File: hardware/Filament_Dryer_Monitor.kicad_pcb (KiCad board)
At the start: 4 copper layers, 91 x 52 mm, 95 parts, among them J1 DC Connector, J2 USB_C_Receptacle_USB2.0_16P, J3 Sensor, J4 Display, J5 Heater Connector, J6 Fan Connector, J7 NTC Connector, Q1 DMP6180SK3-13, Q2 MMBT3904, Q3 MMBT3904, Q4 IRLR3636TRPBF, Q5 CJ2310, Q6 MMBT3904, U1 AP66200, U2 CP2102N-A02-GQFN28R, U3 USBLC6-2SC6, U4 ESP32-WROOM-32E-N4

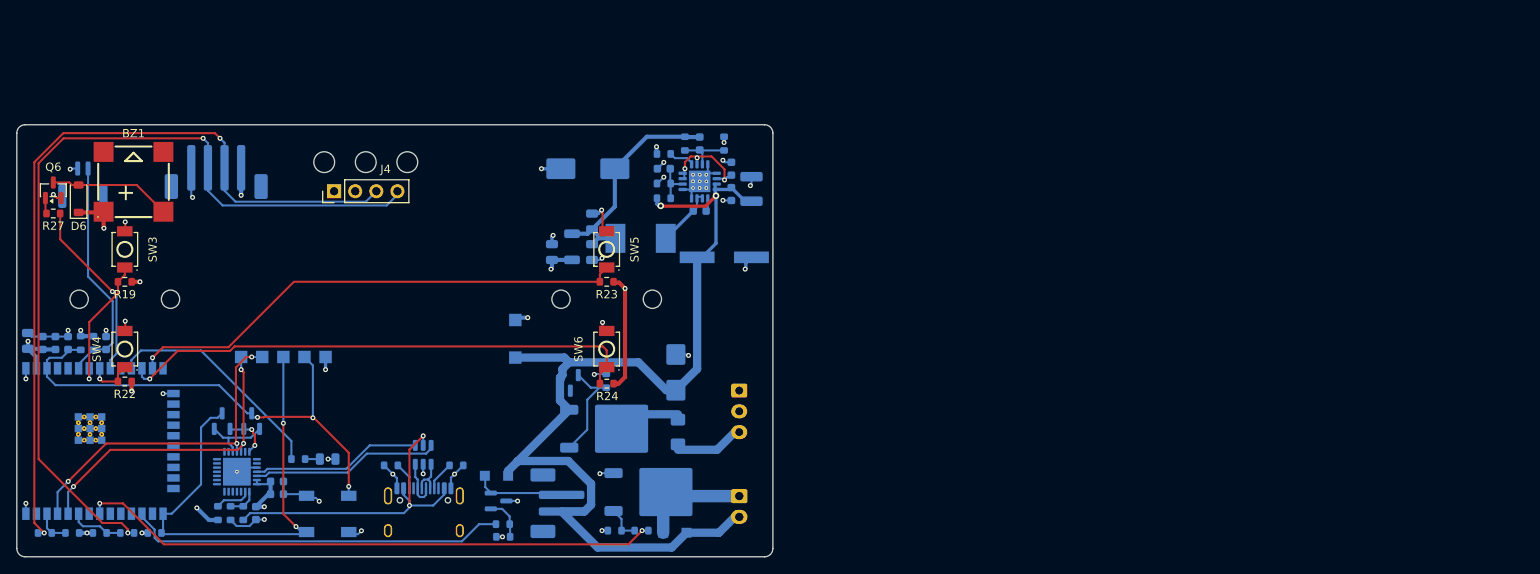
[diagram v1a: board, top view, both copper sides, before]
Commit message: Sync PCB with L7987L schematic
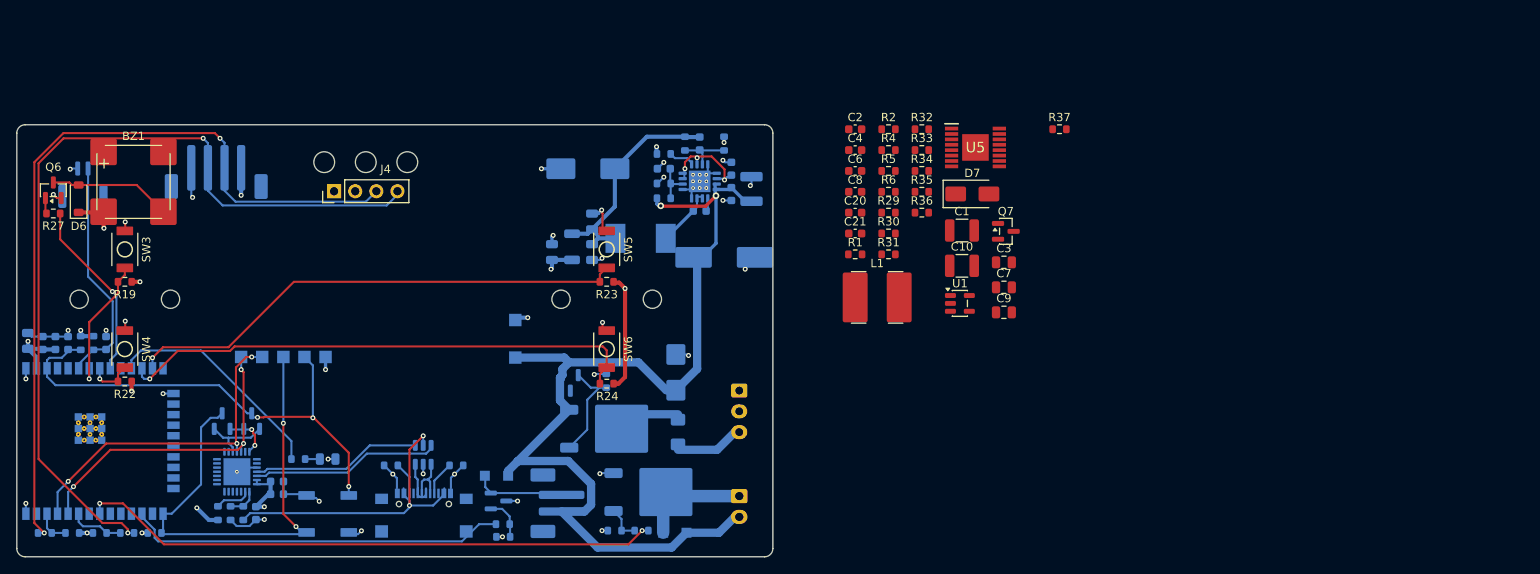
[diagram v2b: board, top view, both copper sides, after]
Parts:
- added C1: 10u, Capacitor_SMD:C_1210_3225Metric, F.Cu at (213.8, 92.7)
- added C10: 47u, Capacitor_SMD:C_1210_3225Metric, F.Cu at (213.8, 97.0)
- added C2: 100n, Capacitor_SMD:C_0603_1608Metric, F.Cu at (200.9, 80.5)
- added C20: 560p, Capacitor_SMD:C_0603_1608Metric, F.Cu at (200.9, 90.6)
- added C21: 1u, Capacitor_SMD:C_0603_1608Metric, F.Cu at (200.9, 93.1)
- added C3: 1u, Capacitor_SMD:C_0805_2012Metric, F.Cu at (218.8, 96.6)
- added C4: 33n, Capacitor_SMD:C_0603_1608Metric, F.Cu at (200.9, 83.0)
- added C6: 100n, Capacitor_SMD:C_0603_1608Metric, F.Cu at (200.9, 85.6)
- added C7: 330n, Capacitor_SMD:C_0805_2012Metric, F.Cu at (218.8, 99.6)
- added C8: 39p, Capacitor_SMD:C_0603_1608Metric, F.Cu at (200.9, 88.1)
- added C9: 18n, Capacitor_SMD:C_0805_2012Metric, F.Cu at (218.8, 102.6)
- added D7: STPS2L60A, Diode_SMD:D_SMA, F.Cu at (215.0, 88.3)
- added L1: 15u, FilamentDryer:L_Bourns_SRN6045, F.Cu at (203.6, 100.8)
- added Q7: MMBT3904, Package_TO_SOT_SMD:SOT-23, F.Cu at (219.0, 92.8)
- added R1: 270k, Resistor_SMD:R_0603_1608Metric, F.Cu at (200.9, 95.6)
- added R2: 22k, Resistor_SMD:R_0603_1608Metric, F.Cu at (204.9, 80.5)
- added R29: 47k5, Resistor_SMD:R_0603_1608Metric, F.Cu at (204.9, 90.6)
- added R30: 47k, Resistor_SMD:R_0603_1608Metric, F.Cu at (204.9, 93.1)
- added R31: 100k, Resistor_SMD:R_0603_1608Metric, F.Cu at (204.9, 95.6)
- added R32: 15k, Resistor_SMD:R_0603_1608Metric, F.Cu at (208.9, 80.5)
- added R33: 16k, Resistor_SMD:R_0603_1608Metric, F.Cu at (208.9, 83.0)
- added R34: 16k, Resistor_SMD:R_0603_1608Metric, F.Cu at (208.9, 85.6)
- added R35: 1k13, Resistor_SMD:R_0603_1608Metric, F.Cu at (208.9, 88.1)
- added R36: 49k9, Resistor_SMD:R_0603_1608Metric, F.Cu at (208.9, 90.6)
- added R37: 100k, Resistor_SMD:R_0603_1608Metric, F.Cu at (225.5, 80.5)
- added R4: 47k, Resistor_SMD:R_0603_1608Metric, F.Cu at (204.9, 83.0)
- added R5: 100k, Resistor_SMD:R_0603_1608Metric, F.Cu at (204.9, 85.6)
- added R6: 100k, Resistor_SMD:R_0603_1608Metric, F.Cu at (204.9, 88.1)
- added U1: TLV1701, Package_TO_SOT_SMD:SOT-23-5, F.Cu at (213.5, 101.5)
- added U5: L7987L, SamacSys_Parts:SOP65P640X120-17N, F.Cu at (215.4, 82.7)
- BZ1: value MLT-8530 -> LD-BZEL-T67-0808; footprint JLCPCB:BUZ-SMD_4P-L8.5-W8.5-P8.50-BR -> FilamentDryer:BUZ_Loudity_SMT67_8.5x8.5
- C5: footprint JLCPCB:CAP-SMD_BD8.0-L8.3-W8.3-FD -> FilamentDryer:CP_Panasonic_F_8x10.2
- D1: value BZX84C15 -> BZX84C15-7-F
- FB1: value HCB3216KF-601T30 -> BLM31KN601SH1L
- J2: footprint FilamentDryer:USB_C_Receptacle_HRO_TYPE-C-31-M-12 -> FilamentDryer:USB_C_GCT_USB4216-03-A
- Q1: value DMP6180SK3-13 -> NTD20P06LT4G
- Q5: value CJ2310 -> IRLML2060TRPBF
- SW1, SW2, SW3, SW4, SW5, SW6: footprint JLCPCB:SW-SMD_L3.9-W3.0-P4.45 -> FilamentDryer:SW_GCT_SWT0110
- U2: value CP2102N-A02-GQFN28R -> CP2102-GM; footprint FilamentDryer:CP2102N_GQFN28_5x5mm_P0.5mm_EP3.35x3.35mm -> FilamentDryer:CP2102_GM_QFN28_5x5_P0.5_EP3.25
- U3: value USBLC6-2SC6 -> AKS1201
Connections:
- D1 pad 1: 24V_PROT -> /Power/GATE_Q1
- D1 pad 2: /Power/GATE_Q1 -> unconnected-(D1-NC-Pad2)
- D1 pad 3: (no net) -> 24V_PROT
- Q5 pad 2: Net-(D5-A) -> GND
- Q5 pad 3: GND -> Net-(D5-A)
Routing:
- net Net-(D5-A): track 11.0 -> 12.3 mm, vias 0 -> 1
- net GND: track 72.0 -> 70.6 mm, vias 46 -> 45

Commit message: first buck converter placement
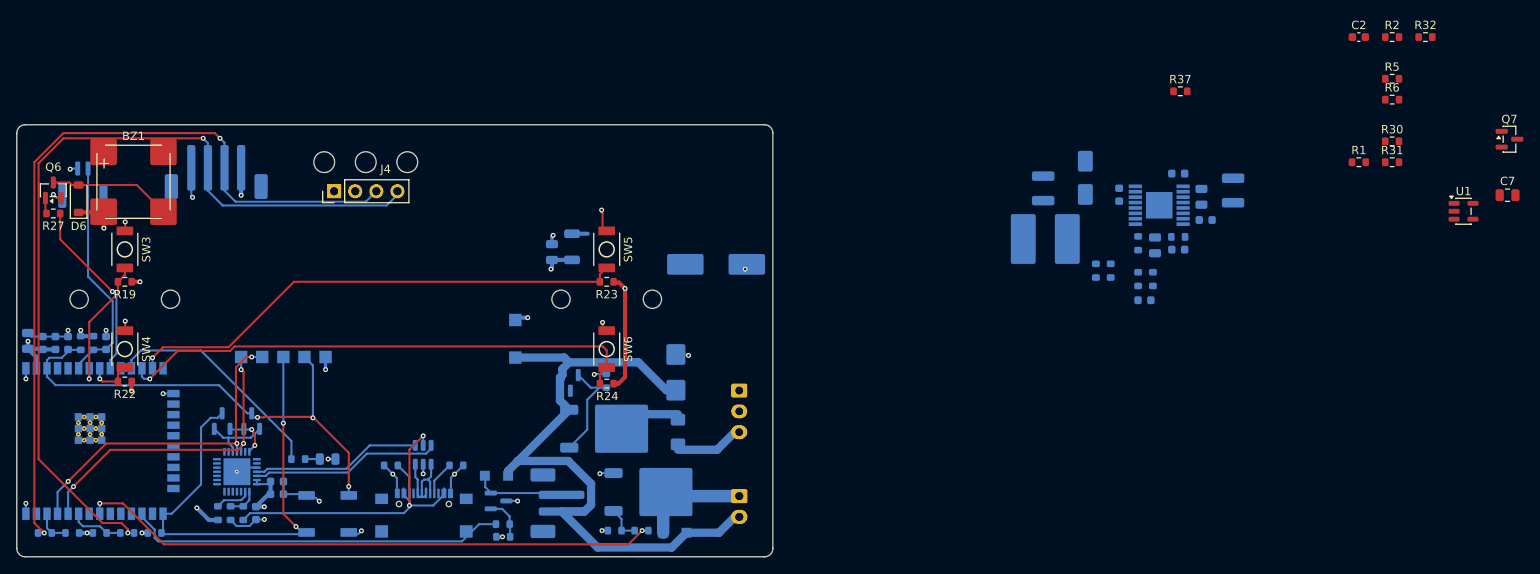
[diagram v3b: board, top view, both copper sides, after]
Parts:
- removed the C1 at (177.9, 85.3)
- removed the C10 at (168.7, 85.3)
- removed the C2 at (186.0, 85.3)
- removed the C3 at (182.2, 90.4)
- removed the C4 at (182.2, 82.3)
- removed the C6 at (169.2, 91.6)
- removed the C7 at (188.4, 87.7)
- removed the C8 at (169.2, 95.3)
- removed the C9 at (186.0, 88.3)
- removed the L1 at (175.1, 93.7)
- removed the R1 at (177.9, 88.8)
- removed the R2 at (177.9, 87.1)
- removed the R4 at (177.9, 83.5)
- removed the R5 at (180.4, 82.3)
- removed the R6 at (185.1, 82.3)
- removed the U1 at (182.2, 86.8)
- C1, C10, C20, C21, C3, C4, C6, C8, C9, D7, L1, R29, R33, R34, R35, R36, R4, U5: moved to B.Cu
- moved U1 61.6 mm to (274.1, 90.4)
- moved C2 61.6 mm to (261.5, 69.4)
- moved Q7 61.6 mm to (279.7, 81.7)
- moved R1 61.6 mm to (261.5, 84.5)
- moved C7 61.6 mm to (279.4, 88.5)
- moved R2 61.6 mm to (265.5, 69.4)
- moved R30 61.6 mm to (265.5, 82.0)
- moved R31 61.6 mm to (265.5, 84.5)
- moved R32 61.6 mm to (269.5, 69.4)
- moved R5 61.6 mm to (265.5, 74.5)
- moved R6 61.6 mm to (265.5, 77.0)
- moved C4 43.0 mm to (243.1, 91.5)
- moved C21 39.5 mm to (239.8, 85.9), turned to 180 degrees
- moved C8 39.5 mm to (239.8, 95.0), turned to 180 degrees
- moved C20 36.4 mm to (235.7, 101.1), turned to 180 degrees
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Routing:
- net 24V_PROT: track 120.4 -> 79.7 mm, vias 2 -> 0
- net /Power/3V3_BUCK: track 27.4 -> 1.89 mm
- net GND: track 70.6 -> 55.5 mm, vias 45 -> 28
- net /Power/VCC_AP66200: track 12.0 -> 0.00 mm, vias 3 -> 0
- net Net-(C3-Pad1): track 7.22 -> 0.00 mm
- net Net-(U1-FB): track 6.81 -> 0.00 mm
- net /Power/EN_BUCK: track 5.25 -> 0.00 mm
- net Net-(U1-PG): track 3.35 -> 0.00 mm
- net Net-(U1-BST): track 1.79 -> 0.00 mm
- net 3V3_MCU: track 52.3 -> 51.5 mm, vias 14 -> 13

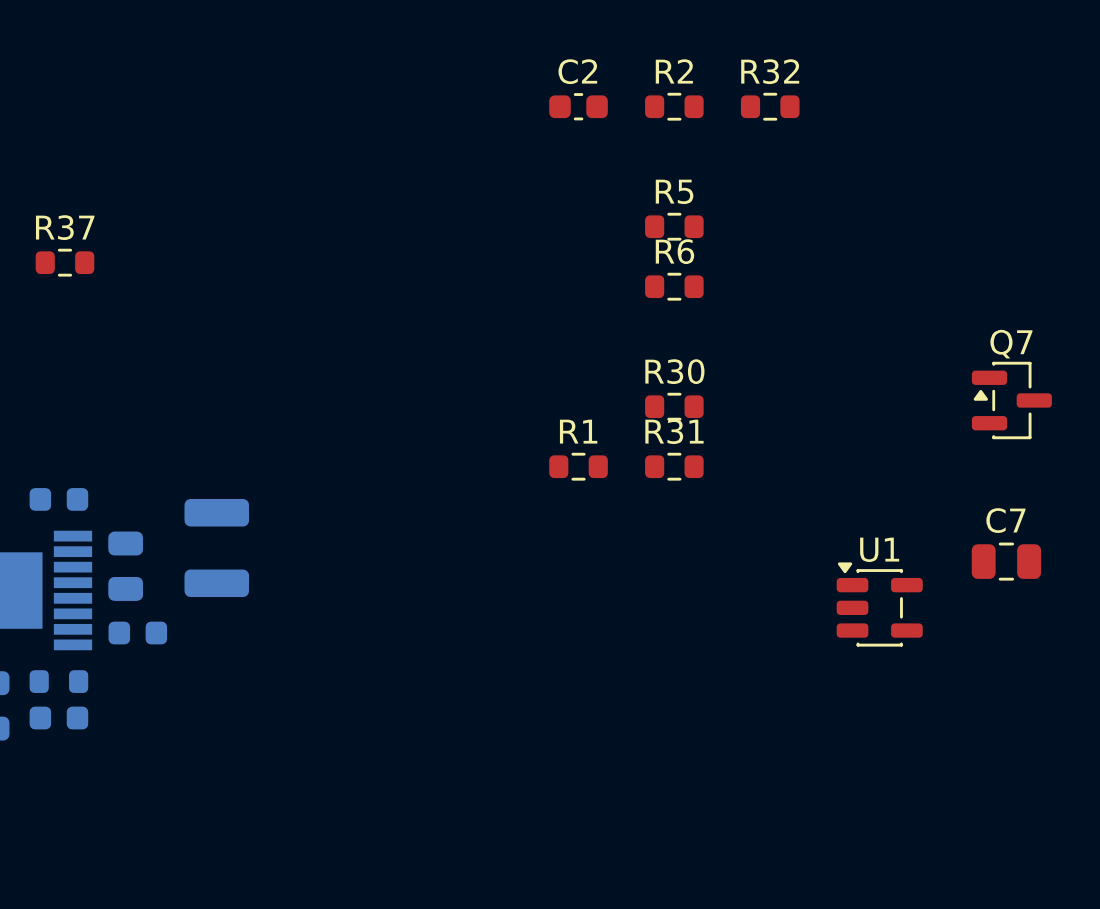
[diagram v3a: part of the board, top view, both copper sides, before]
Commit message: Place power components on bottom
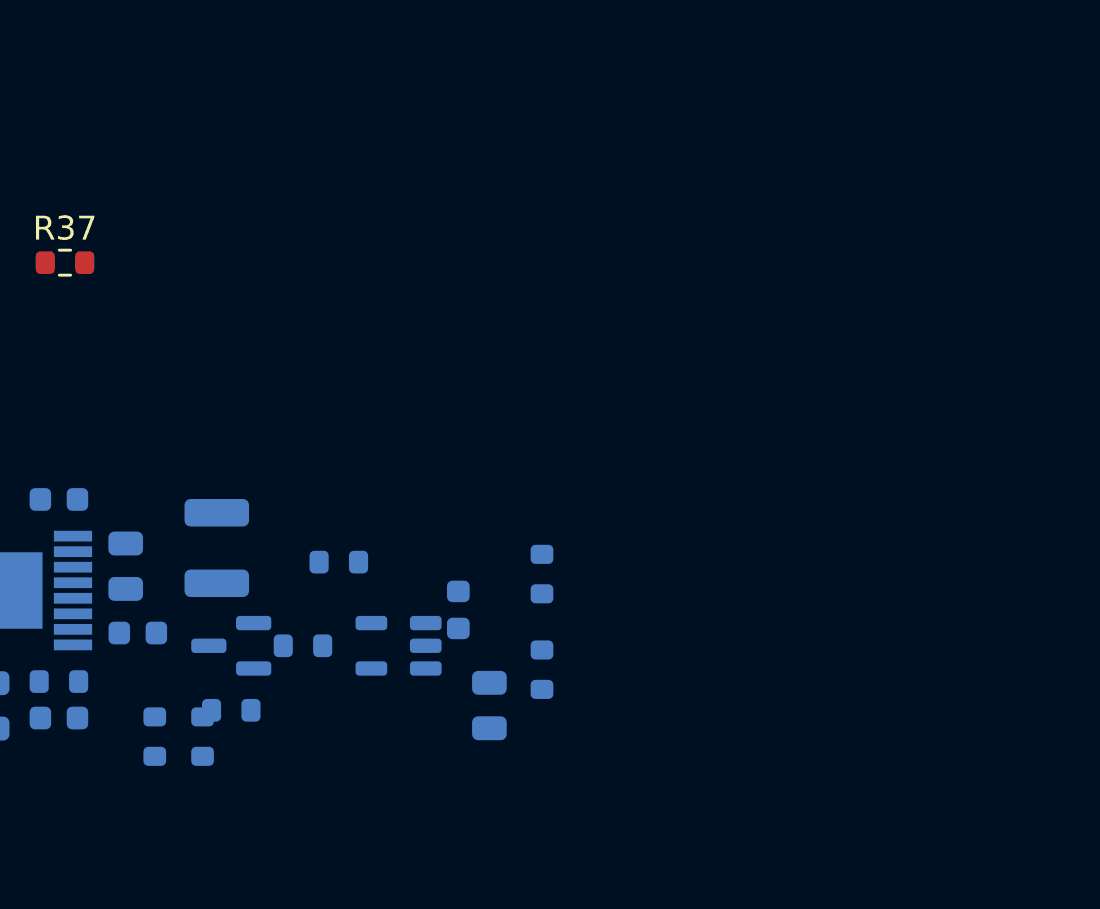
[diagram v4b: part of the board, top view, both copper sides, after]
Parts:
- C2, C7, Q7, R1, R2, R30, R31, R32, R5, R6, U1: moved to B.Cu
- moved R32 35.5 mm to (245.8, 95.8), turned to 90 degrees
- moved Q7 34.2 mm to (247.0, 92.0), turned to 180 degrees
- moved R31 24.5 mm to (243.8, 95.8), turned to 90 degrees
- moved R2 24.2 mm to (260.0, 93.0), turned to 90 degrees
- moved R30 22.5 mm to (247.0, 94.7)
- moved C7 22.5 mm to (257.8, 94.5), turned to 90 degrees
- moved C2 21.6 mm to (256.5, 90.5), turned to 90 degrees
- moved R6 21.6 mm to (250.0, 92.0)
- moved U1 20.2 mm to (254.0, 92.0), turned to 180 degrees
- moved R5 19.8 mm to (251.5, 88.5)
- moved R1 4.75 mm to (260.0, 89.0), turned to 90 degrees
